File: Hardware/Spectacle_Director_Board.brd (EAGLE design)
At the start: 25.4 x 55.9 mm, 67 parts, among them J2 I2C-TRRS, J3 Serial-TRRS, Q1 310mA/60V/1.6Ω, Q2 310mA/60V/1.6Ω, U1 AP2151, U2 ATSAMD21G-A, U3 3.3V, U4 W25Q32FV

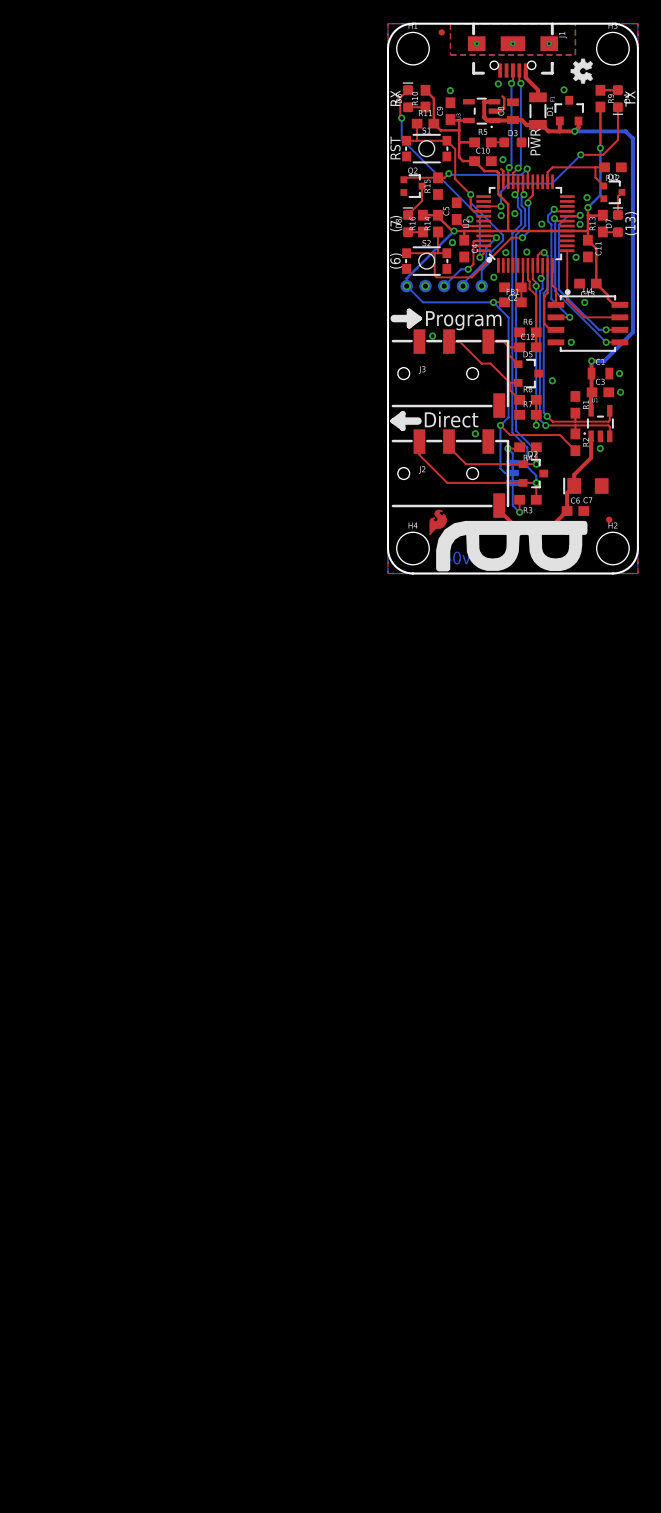
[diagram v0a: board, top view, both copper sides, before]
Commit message: Added FSK demodulation hardware Changed pin assignment of FSK channel to channel with comparator Moved power switch FAULT line to a different pin
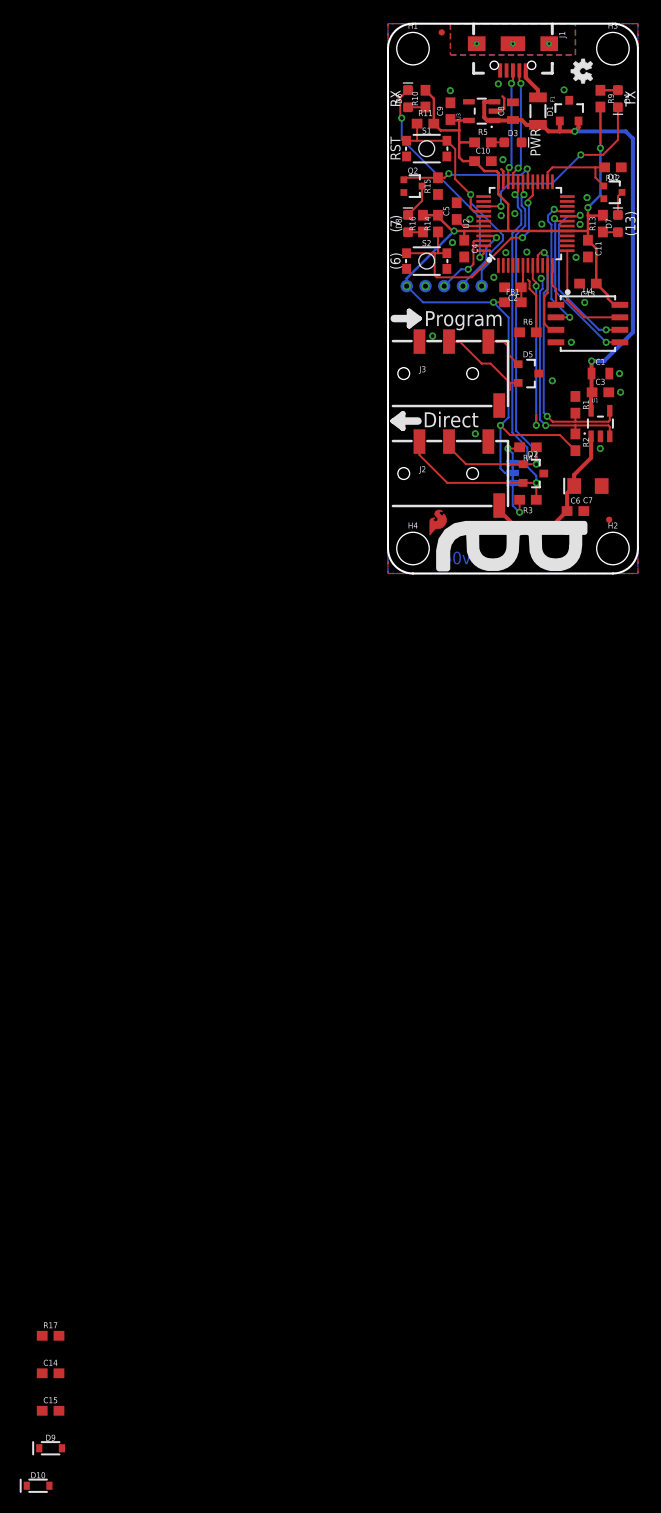
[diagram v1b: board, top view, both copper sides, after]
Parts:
- removed C12: 1.0uF, SparkFun-Capacitors:0603
- removed R7: DNP, SparkFun-Resistors:0603
- removed R8: 0, SparkFun-Resistors:0603
- added C14: 0.22uF, SparkFun-Capacitors:0603
- added C15: 47pF, SparkFun-Capacitors:0603
- added D10, D9: 0.5A/40V/420mV, SparkFun-DiscreteSemi:SOD-323
- added R17: 10k, SparkFun-Resistors:0603
- R6: value 4.7k -> 10k
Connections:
- net 3.3V: now also D9.C, R17.2
- net A1_FSK-RX: now also C14.1, C15.2, D10.C, D9.A, R17.1, U2.10; no longer C12.2, U2.7
- net A2: no longer R7.2, R8.2
- net A4_VOUT_FLG: now also U2.3; no longer U2.10
- net GND: now also C15.1, D10.A; no longer R7.1
- net RING1-RIGHT: no longer R8.1
- net TIP-LEFT: now also C14.2; no longer C12.1
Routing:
- net A1_FSK-RX: track 8.68 -> 5.70 mm
- net A2: track 19.0 -> 17.5 mm
- net RING1-RIGHT: track 10.9 -> 9.50 mm
- net A4_VOUT_FLG: track 25.1 -> 24.0 mm
- net TIP-LEFT: track 5.51 -> 4.44 mm

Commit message: FSK demodulation harware layout
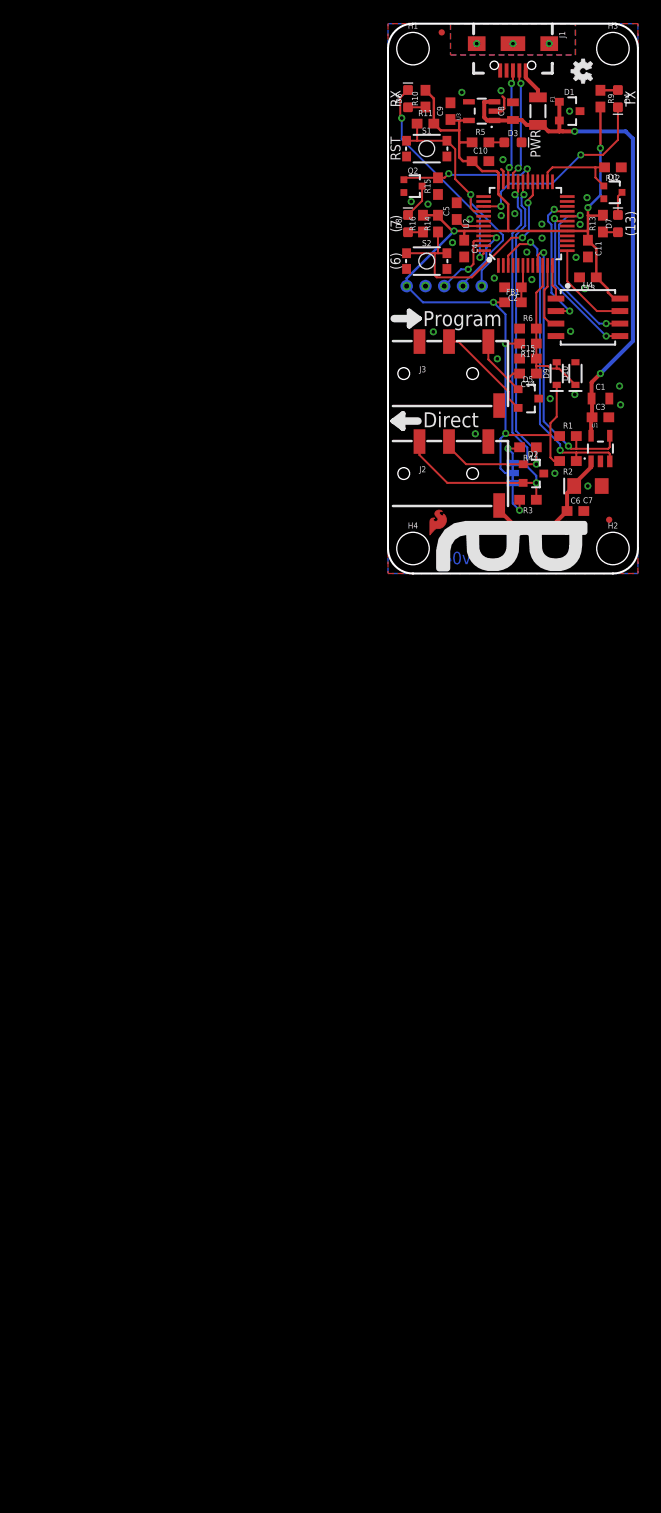
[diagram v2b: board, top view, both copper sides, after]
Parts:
- JP1: value JUMPER-SMT_3_2-NC_TRACE_SILK -> JUMPER-SMT_3_2-NC_TRACE_NO-SILK; device SparkFun-Jumpers:SMT-JUMPER_3_2-NC_TRACE_SILK -> SparkFun-Jumpers:SMT-JUMPER_3_2-NC_TRACE_NO-SILK
- moved D10 125.5 mm to (19.1, 20.3), turned to 90 degrees
- moved D9 120.7 mm to (17.1, 20.3), turned to 90 degrees
- moved C15 117.4 mm to (14.2, 21.8)
- moved C14 112.6 mm to (14.2, 20.3), turned to 180 degrees
- moved R17 111.9 mm to (14.2, 23.4), turned to 180 degrees
- moved LOGO2 3.43 mm to (23.5, 19.6)
- moved R1 3.27 mm to (18.3, 14.0), turned to 0 degrees
- moved U1 2.54 mm to (21.6, 12.7)
- moved C1 2.54 mm to (21.6, 17.8)
- moved C3 2.54 mm to (21.6, 15.9)
- moved D5 2.54 mm to (14.2, 17.8)
- moved R2 2.05 mm to (18.3, 11.4), turned to 180 degrees
- moved C13 0.64 mm to (20.3, 30.1)
- moved U4 0.64 mm to (20.3, 26.0)
- moved R6 0.38 mm to (14.2, 24.9)
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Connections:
- removed net A2: U2.8
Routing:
- net A2: track 17.5 -> 0.00 mm, vias 2 -> 0
- net A1_FSK-RX: track 5.70 -> 16.7 mm
- net A4_VOUT_FLG: track 24.0 -> 33.0 mm
- net 3.3V: track 113.6 -> 118.4 mm, vias 6 -> 7
- net TIP-LEFT: track 4.44 -> 7.52 mm
- net V_USB: track 51.2 -> 53.7 mm
- net VOUT: track 17.1 -> 14.7 mm
- net A3_VOUT_EN: track 27.4 -> 29.3 mm
- net D4_FLASH!HD!: track 11.1 -> 9.73 mm
- net RING1-RIGHT: track 9.50 -> 10.2 mm
- net SPI_MISO: track 14.9 -> 14.3 mm
- net D9_FLASH!CS!: track 4.15 -> 3.51 mm
- net SPI_SCK: track 18.4 -> 17.8 mm
- net SPI_MOSI: track 17.6 -> 16.9 mm
- net D8_FLASH!WP!: track 7.49 -> 6.85 mm
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
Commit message: Minor adjustments post-engineer checklist.
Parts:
- removed C15: 47pF, SparkFun-Capacitors:0603
- removed R16: 330, SparkFun-Resistors:0603
- removed R17: 10k, SparkFun-Resistors:0603
- added C12: 0.1uF, SparkFun-Capacitors:0603
- added R7: 10k, SparkFun-Resistors:0603
- added R8: 330, SparkFun-Resistors:0603
- C11: value 0.1uF -> 47pF
- C13: value 0.1uF -> 0.22uF
- C14: value 0.22uF -> 0.1uF
- D10: value 0.5A/40V/420mV -> GREEN; device SparkFun-DiscreteSemi:SOD-323 -> SparkFun-LED:LED-0603
- D4: value GREEN -> 0.5A/40V/420mV; device SparkFun-LED:LED-0603 -> SparkFun-DiscreteSemi:SOD-323
- D5: value PESD1CAN -> 0.5A/40V/420mV; device SparkFun-DiscreteSemi:SOT23-3 -> SparkFun-DiscreteSemi:SOD-323
- D6: value Yellow -> GREEN
- D7: value BLUE -> PESD1CAN; device SparkFun-LED:LED-0603 -> SparkFun-DiscreteSemi:SOT23-3
- D8: value GREEN -> Yellow
- D9: value 0.5A/40V/420mV -> BLUE; device SparkFun-DiscreteSemi:SOD-323 -> SparkFun-LED:LED-0603
- R10, R13: value 330 -> 10k
- R11, R14: value 10k -> 100k
- R12, R15: value 100k -> 330
- R5: value 1k -> 10k
- R6: value 10k -> 1k
- moved D4 28.6 mm to (17.1, 20.3), turned to 90 degrees
- moved D10 22.8 mm to (2.03, 35.6)
- moved D6 21.3 mm to (23.4, 48.3), turned to 270 degrees
- moved R5 21.0 mm to (14.2, 23.4), turned to 180 degrees
- moved D7 20.0 mm to (14.2, 17.8), turned to 270 degrees
- moved R11 19.6 mm to (22.9, 41.3), turned to 180 degrees
- moved R6 19.5 mm to (9.40, 43.8)
- moved R9 17.8 mm to (3.81, 48.3), turned to 90 degrees
- moved R13 16.8 mm to (5.08, 35.6)
- moved D9 16.5 mm to (23.4, 35.6)
- moved C11 12.7 mm to (14.2, 21.8), turned to 0 degrees
- moved D8 12.7 mm to (2.03, 48.3)
- moved C13 11.5 mm to (14.2, 20.3)
- moved C14 11.5 mm to (20.3, 30.1)
- moved R12 5.80 mm to (21.8, 35.6), turned to 90 degrees
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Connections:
- net !RESET: now also R10.1; no longer R11.1
- net 3.3V: now also C12.1, C14.1, D4.C, R12.2, R15.2, R5.2, R6.1, R8.2; no longer C11.1, C13.1, D9.C, R11.2, R14.2, R16.2, R17.2, R5.1
- net A1_FSK-RX: now also C11.2, C13.1, D4.A, D5.C, R5.1, R7.2; no longer C14.1, C15.2, D10.C, D9.A, R17.1, R6.2
- net D13_LED1: now also R11.2; no longer R12.2
- net D6_BTN: now also R13.1; no longer R14.1
- net D7_LED2: now also R14.2; no longer R15.2
- net GND: now also C11.1, C12.2, C14.2, D5.A, D7.3, R11.1, R14.1, R7.1; no longer C11.2, C13.2, C15.1, D10.A, D5.3, R12.1, R15.1, R6.1
- net N$1: now also D10.A, R15.1; no longer D8.A, R16.1
- net N$10: now also D9.C; no longer D7.C
- net N$11: now also D6.A, R8.1; no longer D4.A, R9.1
- net N$12: now also D8.A, R9.1; no longer D6.A, R10.1
- net N$2: now also R6.2; no longer R5.2
- net N$7: now also D10.C; no longer D8.C
- net N$9: now also D9.A, R12.1; no longer D7.A, R13.1
- net RING1-RIGHT: now also D7.2; no longer D5.2
- net RX_LED: now also D8.C; no longer D6.C
- net TIP-LEFT: now also C13.2, D7.1; no longer C14.2, D5.1
- net TX_LED: now also D6.C; no longer D4.C

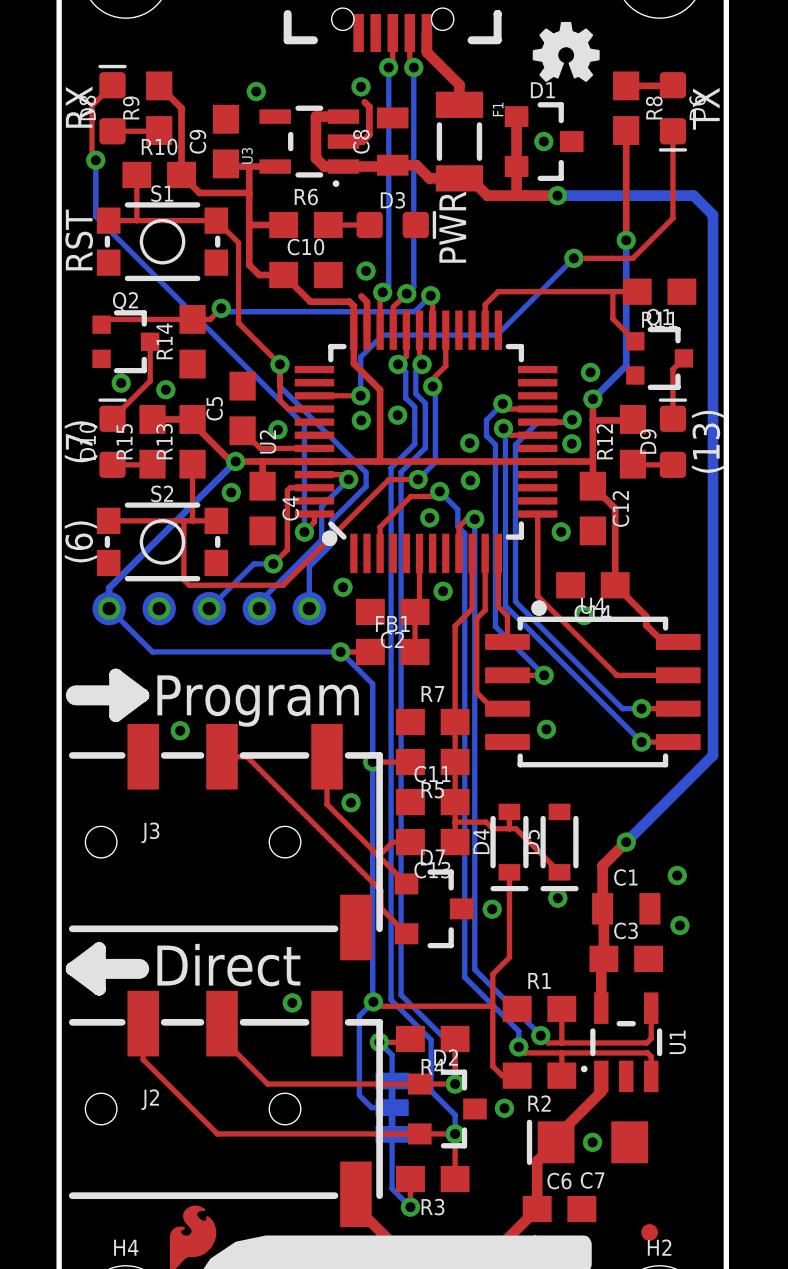
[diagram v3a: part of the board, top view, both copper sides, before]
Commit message: Adding UART test points, 32.768kHz RTC crystal
- Moved flash down about 0.1" to accomodate uart test points
- Moved SWD test points to accomodate RTC crystal
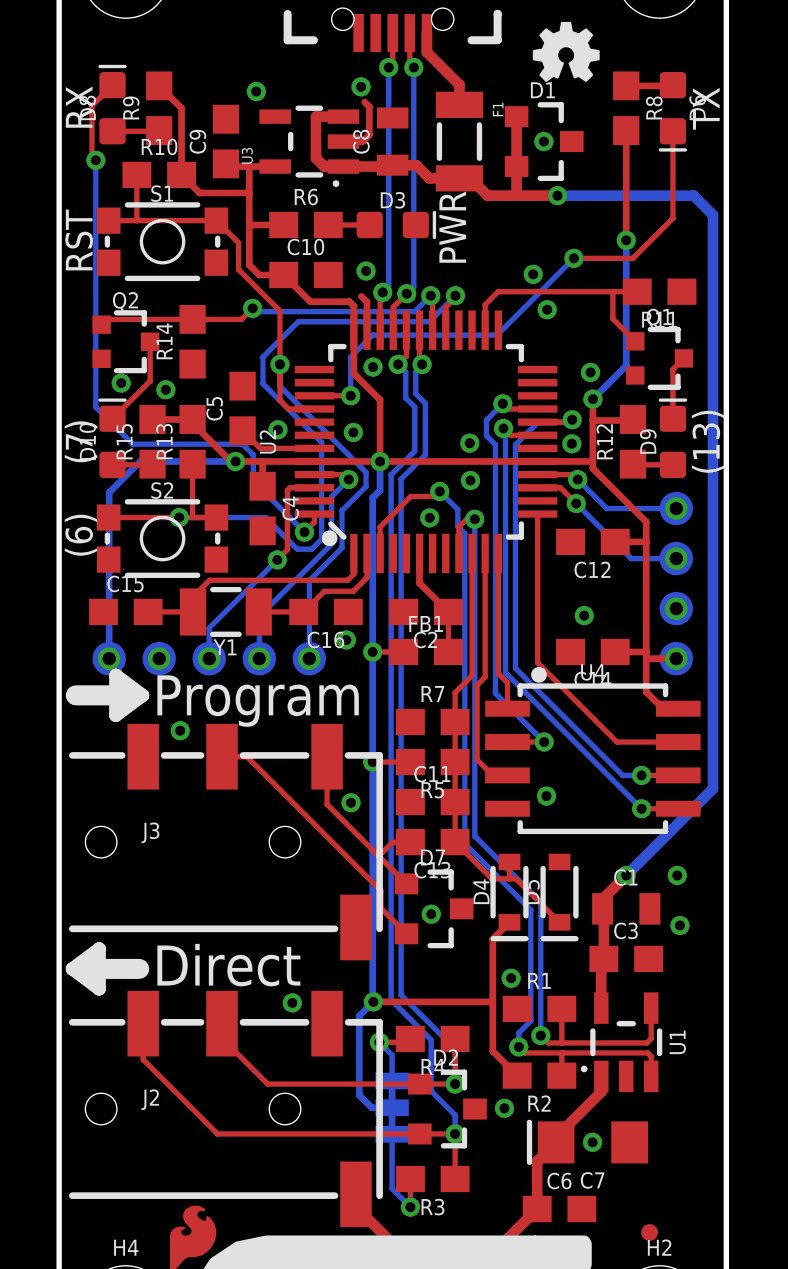
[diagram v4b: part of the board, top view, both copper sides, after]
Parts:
- added C15, C16: 15pF, SparkFun-Capacitors:0603
- added TP6, TP7, TP8, TP9: TP-GND, SparkFun-Connectors:PAD.03X.05
- added Y1: 32.768kHz, SparkFun-Clocks:CRYSTAL-SMD-3.2X1.5MM
- moved C14 2.54 mm to (20.3, 27.6)
- moved U4 2.54 mm to (20.3, 23.5)
- moved D4 1.91 mm to (17.1, 18.4)
- moved D5 1.91 mm to (19.1, 18.4)
- moved TP1 1.91 mm to (5.71, 27.3)
- moved TP2 1.91 mm to (7.62, 27.3)
- moved TP3 1.91 mm to (9.53, 27.3)
- moved TP4 1.91 mm to (1.91, 27.3)
- moved TP5 1.91 mm to (3.81, 27.3)
- moved C12 1.27 mm to (20.3, 31.8), turned to 180 degrees
- moved C2 1.27 mm to (14.0, 29.1)
- moved FB1 1.27 mm to (14.0, 27.6)
- moved S2 0.13 mm to (3.94, 31.9)
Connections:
- new net D0/RXI: TP8.P$1, U2.16
- new net D1/TXO: TP7.P$1, U2.15
- new net N$3: C15.2, U2.1, Y1.P$2
- new net N$6: C16.2, U2.2, Y1.P$1
- net 3.3V: now also TP6.P$1
- net GND: now also C15.1, C16.1, TP9.P$1
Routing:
- net N$3: track 0.00 -> 10.1 mm
- net D1/TXO: track 0.00 -> 6.39 mm, vias 0 -> 2
- net D0/RXI: track 0.00 -> 5.81 mm, vias 0 -> 2
- net N$6: track 0.00 -> 5.58 mm
- net 3.3V: track 118.4 -> 123.6 mm, vias 7 -> 9
- net D6_BTN: track 25.6 -> 30.1 mm
- net D9_FLASH!CS!: track 3.51 -> 6.05 mm
- net D4_FLASH!HD!: track 9.73 -> 12.3 mm
- net SPI_SCK: track 17.8 -> 20.3 mm
- net SPI_MISO: track 14.3 -> 16.9 mm
- net SPI_MOSI: track 16.9 -> 19.5 mm
- net D8_FLASH!WP!: track 6.85 -> 9.38 mm
- net RX_LED: track 21.5 -> 24.0 mm
- net SWCLK: track 7.70 -> 9.85 mm
- net !RESET: track 26.7 -> 28.6 mm
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
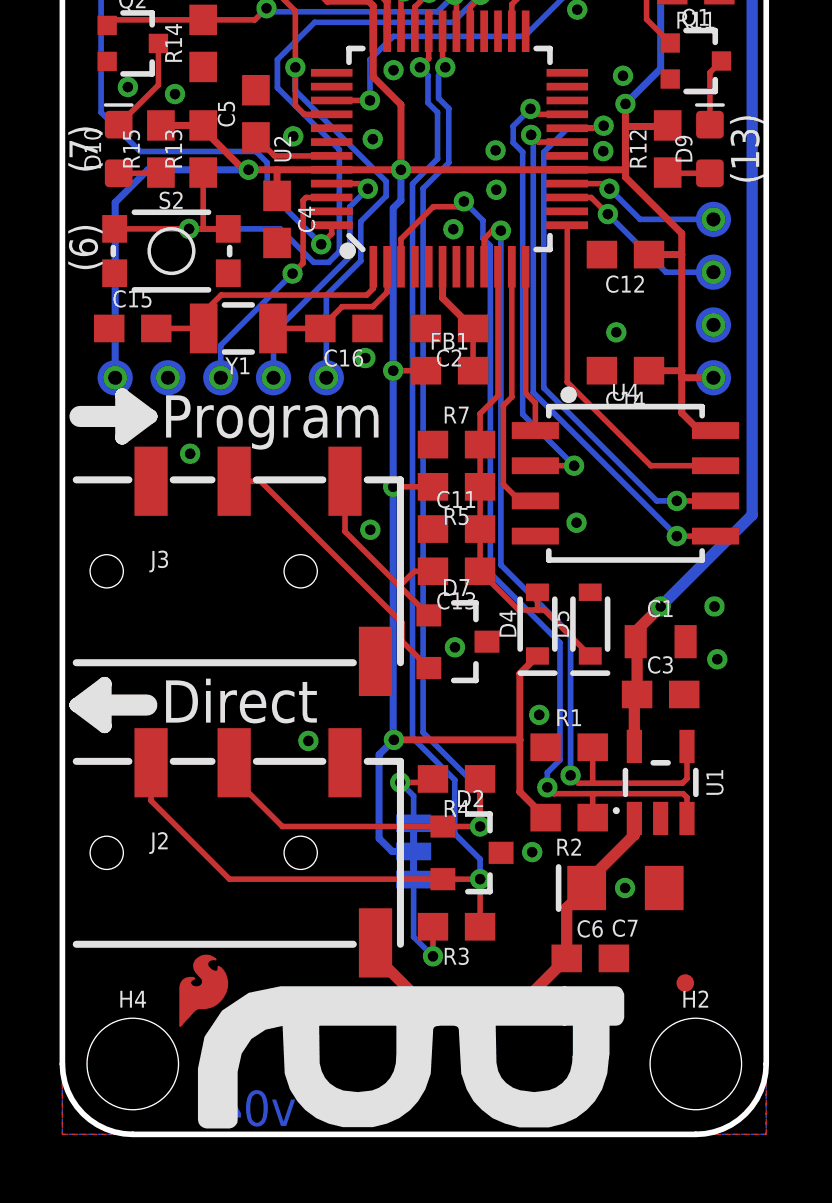
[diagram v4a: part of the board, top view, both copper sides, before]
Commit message: Spacing test points by 2mm, increasing via drill size.
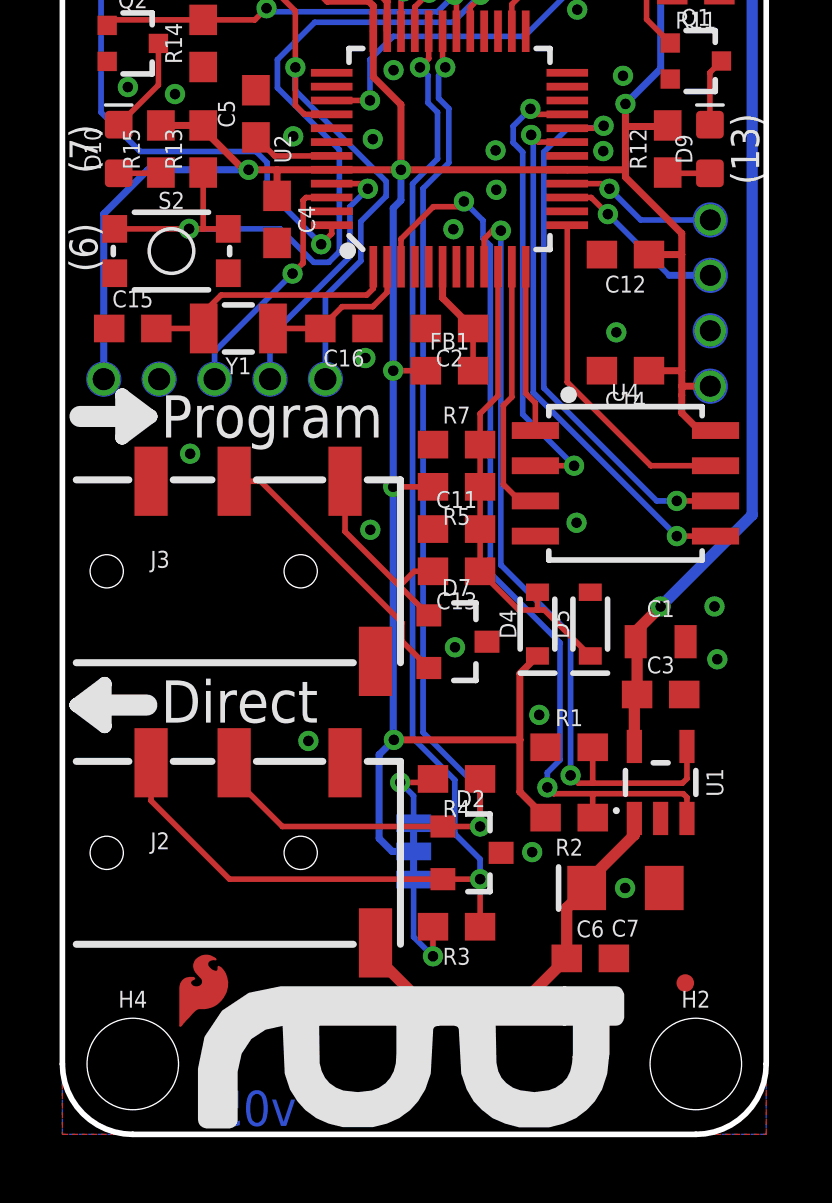
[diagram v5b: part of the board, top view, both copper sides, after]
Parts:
- moved TP4 0.42 mm to (1.49, 27.3)
- moved TP6 0.33 mm to (23.4, 27.0)
- moved TP5 0.32 mm to (3.49, 27.3)
- moved TP9 0.24 mm to (23.4, 29.0)
- moved TP1 0.23 mm to (5.49, 27.3)
- moved TP7 0.16 mm to (23.4, 31.0)
- moved TP2 0.14 mm to (7.49, 27.3)
- moved TP8 0.12 mm to (23.4, 33.0)
- moved TP3 0.06 mm to (9.49, 27.3)
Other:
- board text added: "v05"
- board text removed: "v04"
